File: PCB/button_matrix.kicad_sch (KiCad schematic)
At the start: 12 parts

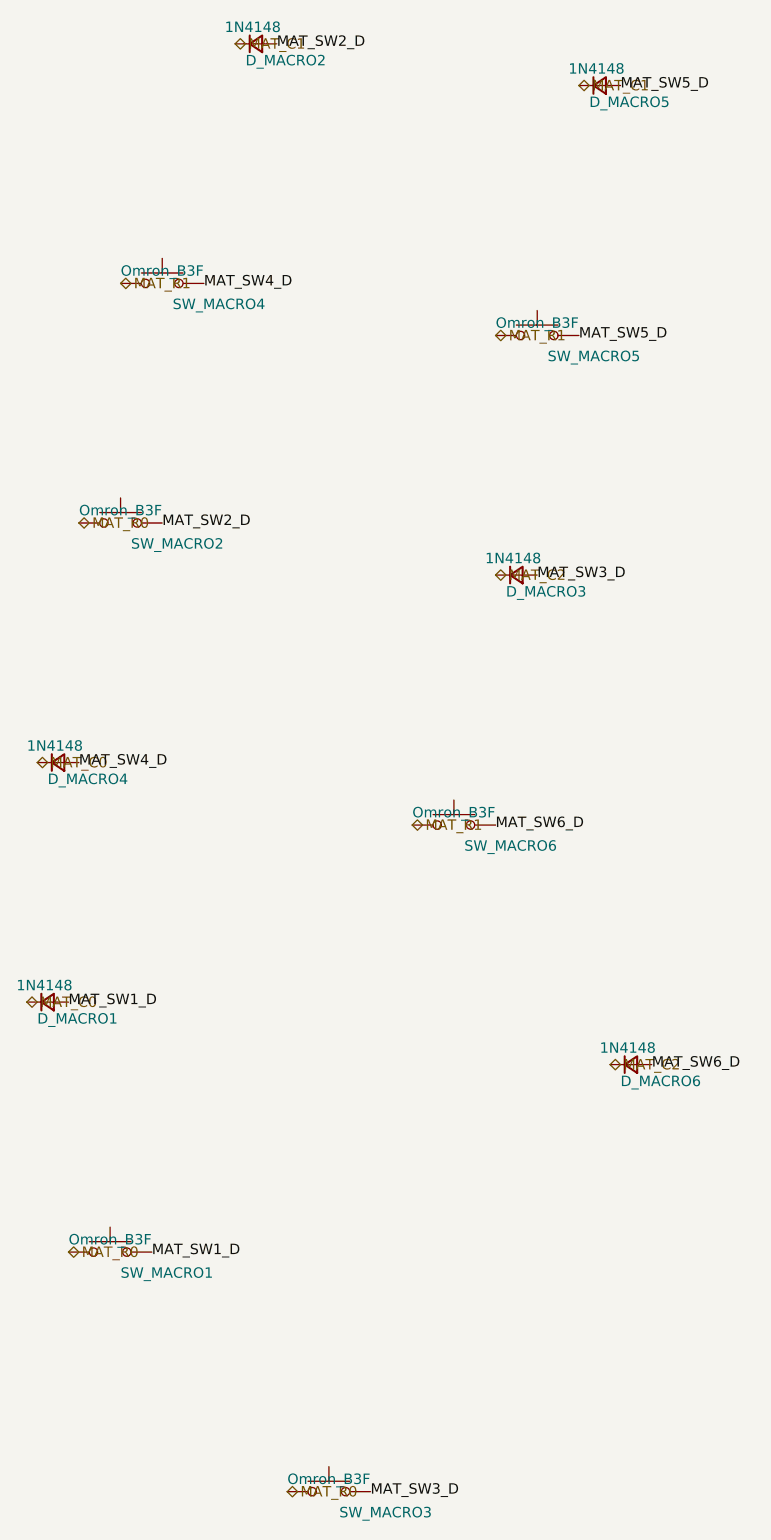
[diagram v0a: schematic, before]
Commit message: refactor: erc is clean
This gets the schematic as clean as it can be.
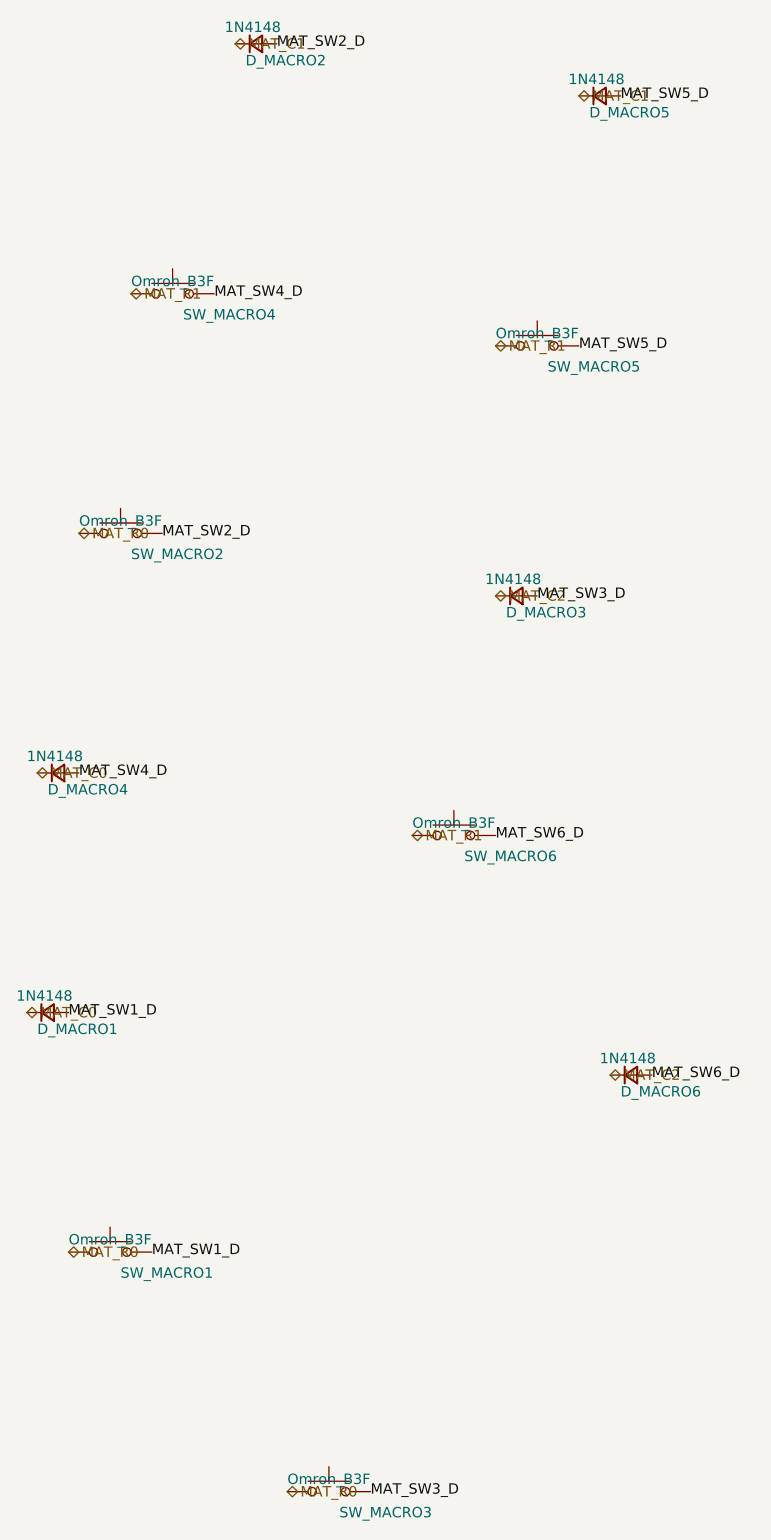
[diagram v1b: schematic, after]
